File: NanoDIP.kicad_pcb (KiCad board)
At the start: 2 copper layers, 71.1 x 23.9 mm, 13 parts, among them SW1 SW_Push, U1 LM7805_TO220, U2 ATMEGA328P-PU, Y1 16 MHz

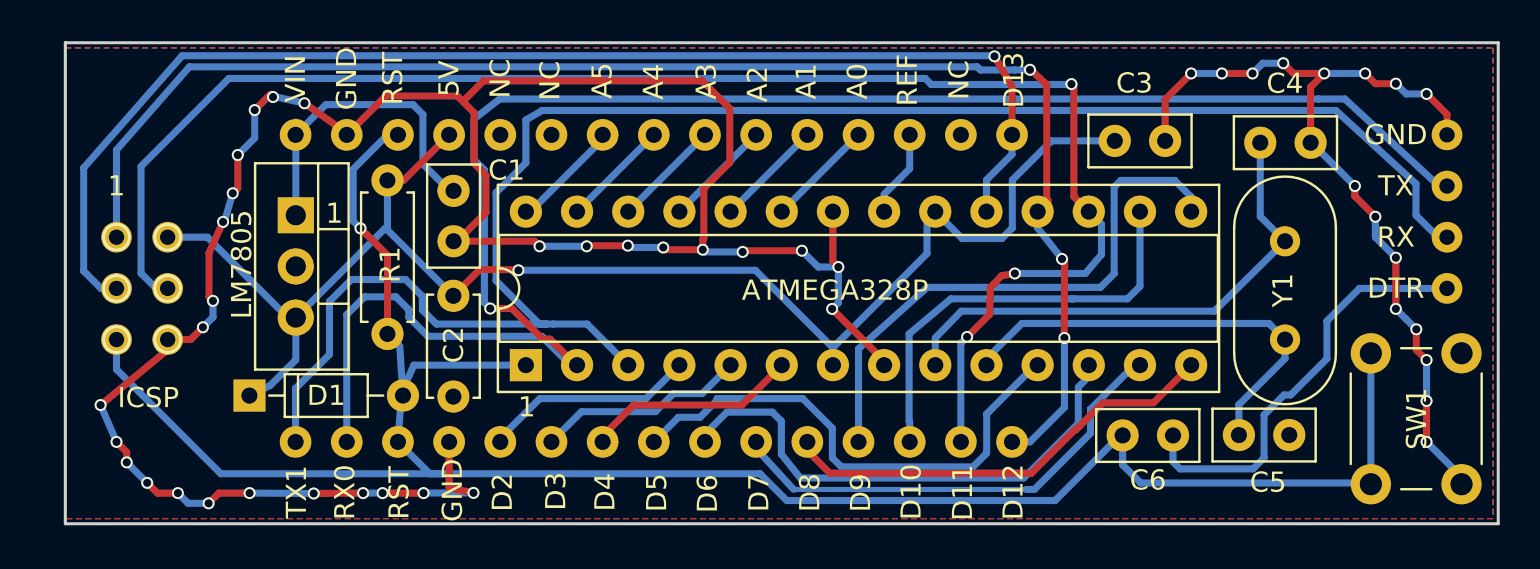
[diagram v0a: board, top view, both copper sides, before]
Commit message: Added 5V pin to program header
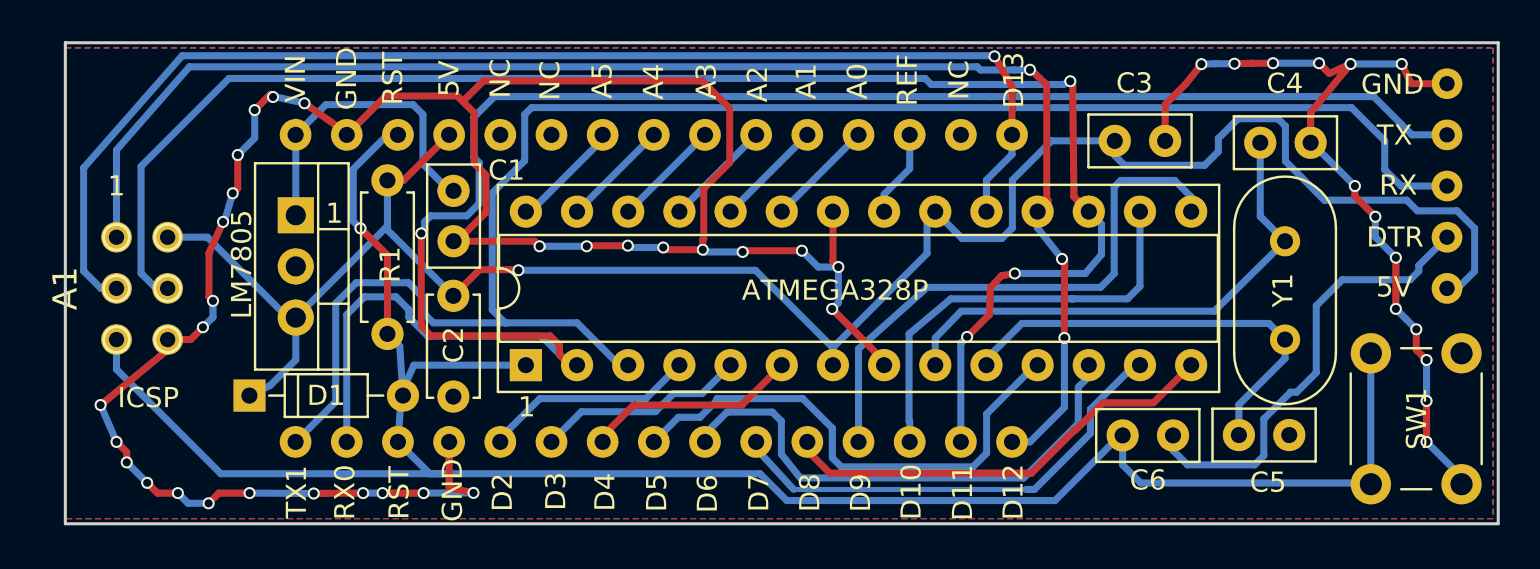
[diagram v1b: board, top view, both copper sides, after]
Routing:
- net +5V: track 77.8 -> 105.1 mm
- net PD0: track 85.3 -> 91.1 mm
- net PD1: track 86.7 -> 84.8 mm
- net Net-(A1-Pad40): track 21.1 -> 22.9 mm
- net GND: track 157.1 -> 156.8 mm, vias 45 -> 43

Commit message: JLCPCB order 2021-10-22
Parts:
- added C7: 100 nF, Capacitors_THT:C_Disc_D5.0mm_W2.5mm_P2.50mm, B.Cu at (165.2, 87.6)
- moved C3 0.91 mm to (173.1, 81.6)
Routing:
- net GND: track 156.8 -> 288.9 mm, vias 43 -> 47
- net PB0: track 22.2 -> 33.4 mm, vias 0 -> 2
- net RESET: track 103.7 -> 111.0 mm
- net +5V: track 105.1 -> 103.8 mm
- net MOSI: track 78.8 -> 80.0 mm
- net PD7: track 23.5 -> 24.3 mm
